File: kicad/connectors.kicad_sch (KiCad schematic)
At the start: 5 parts, among them J1 Conn_Coaxial, J2 Conn_Coaxial, J3 Conn_Coaxial, J4 Conn_Coaxial, J7 Conn_Coaxial

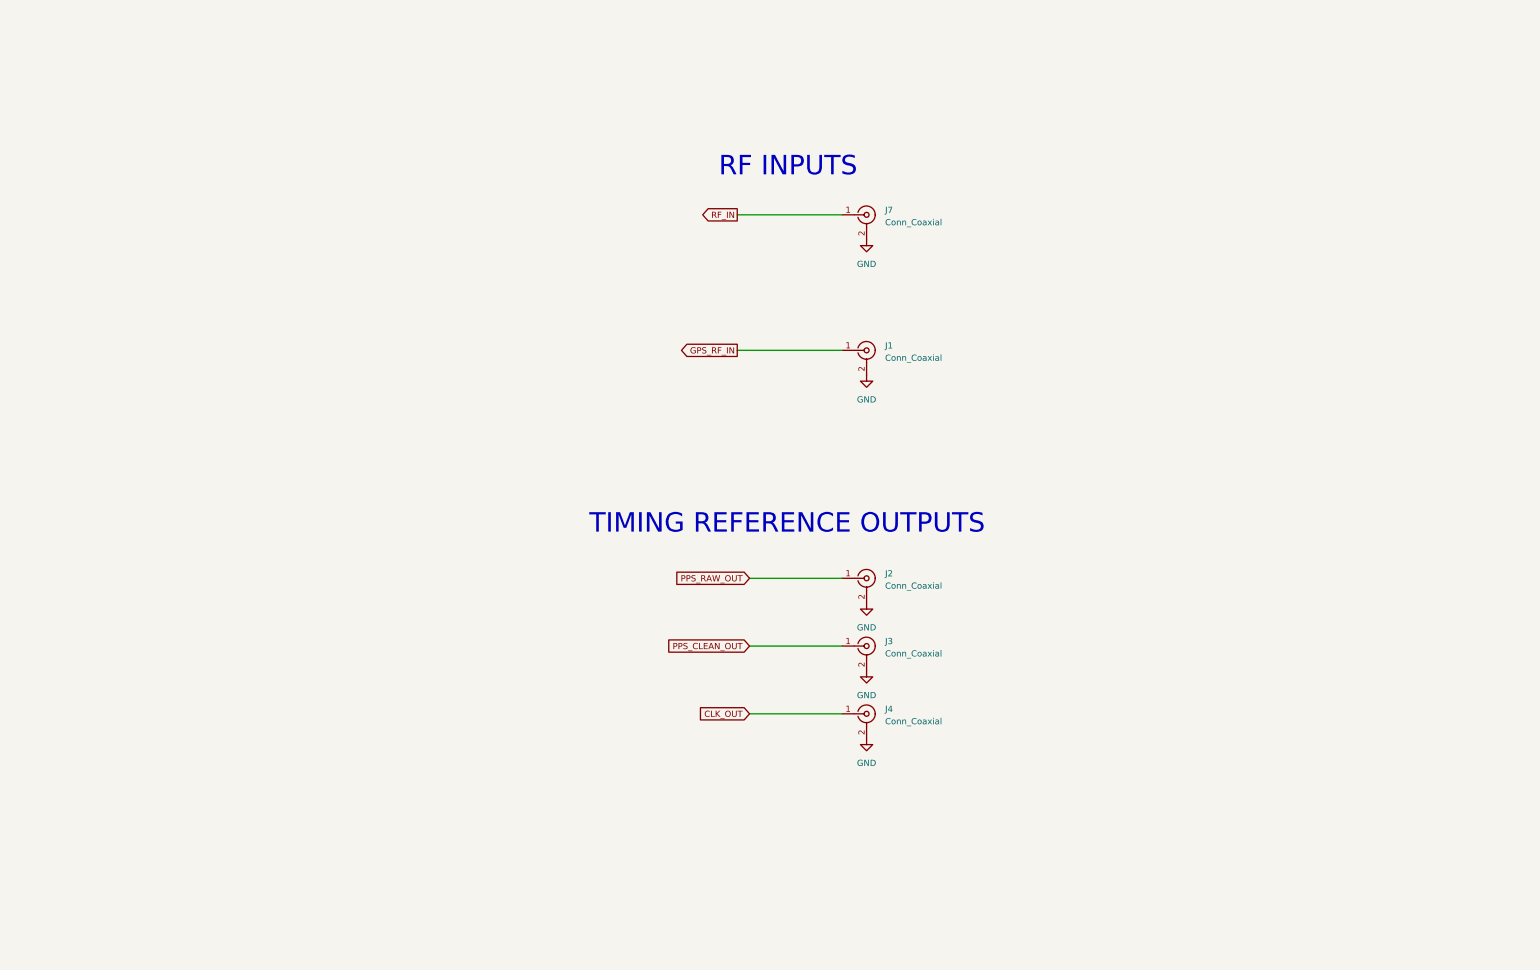
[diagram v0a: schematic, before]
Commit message: swap ice40 for max v, add 1.2v switcher
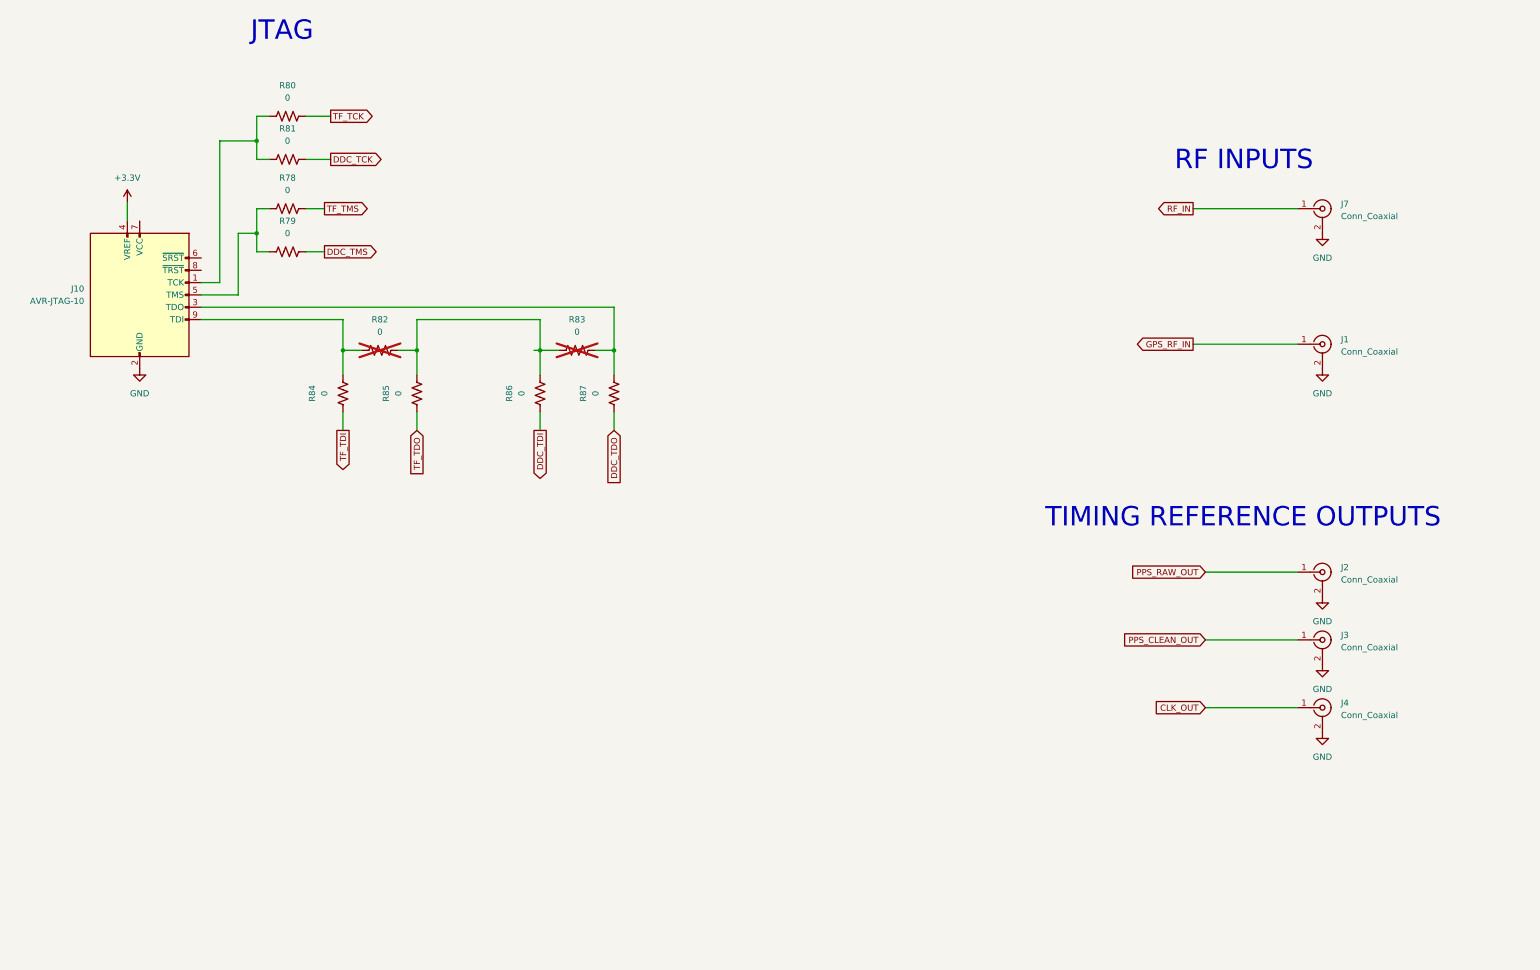
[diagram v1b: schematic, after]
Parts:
- added J10: AVR-JTAG-10, symbol Connector:AVR-JTAG-10
- added R78, R79, R80, R81, R82, R83, R84, R85, R86, R87: 0, symbol Device:R_US
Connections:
- net GND: now also J10.10 (GND), J10.2 (GND)
- new net: J10.5 (TMS), R78.1, R79.1
- new net: J10.1 (TCK), R80.1, R81.1
- new net: J10.3 (TDO), R83.2, R87.2
- new net: J10.9 (TDI), R82.1, R84.2
- new net: R82.2, R83.1, R85.2, R86.2
- new net +3.3V: J10.4 (VREF)
- new net DDC_TCK: R81.2
- new net DDC_TDI: R86.1
- new net DDC_TDO: R87.1
- new net DDC_TMS: R79.2
- new net TF_TCK: R80.2
- new net TF_TDI: R84.1
- new net TF_TDO: R85.1
- new net TF_TMS: R78.2
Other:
- note added: "JTAG"
- moved on the sheet: J1, J2, J3, J4, J7

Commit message: add lte radio and various fixes
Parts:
- added J12: Conn_Coaxial, symbol Connector:Conn_Coaxial
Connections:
- net GND: now also J12.2 (Ext)
- new net LTE_ANT: J12.1 (In)
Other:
- moved on the sheet: J1, J10, R78, R79, R80, R81, R82, R83, R84, R85, R86, R87

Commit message: assign footprints
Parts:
- J1, J12, J2, J3, J4, J7: footprint (none) -> Connector_Coaxial:SMA_Amphenol_901-143_Horizontal
- J10: footprint (none) -> Connector_PinHeader_2.54mm:PinHeader_2x05_P2.54mm_Vertical
- R78, R79, R80, R81, R82, R83, R84, R85, R86, R87: footprint (none) -> Resistor_SMD:R_0603_1608Metric_Pad0.98x0.95mm_HandSolder
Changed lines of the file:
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@@
       (effects (font (size 1.27 1.27)))
     )
-    (property "Footprint" "" (at 108.204 120.904 90)
+    (property "Footprint" "Resistor_SMD:R_0603_1608Metric_Pad0.98x0.95mm_HandSolder" (at 108.204 120.904 90)
       (effects (font (size 1.27 1.27)) hide)
     )
@@
       (effects (font (size 1.27 1.27)) (justify left))
     )
-    (property "Footprint" "" (at 318.77 156.21 0)
+    (property "Footprint" "Connector_Coaxial:SMA_Amphenol_901-143_Horizontal" (at 318.77 156.21 0)
       (effects (font (size 1.27 1.27)) hide)
     )
@@
       (effects (font (size 1.27 1.27)) (justify right))
     )
-    (property "Footprint" "" (at 73.66 135.89 90)
+    (property "Footprint" "Connector_PinHeader_2.54mm:PinHeader_2x05_P2.54mm_Vertical" (at 73.66 135.89 90)
       (effects (font (size 1.27 1.27)) hide)
     )
@@
       (effects (font (size 1.27 1.27)))
     )
-    (property "Footprint" "" (at 133.604 159.766 90)
+    (property "Footprint" "Resistor_SMD:R_0603_1608Metric_Pad0.98x0.95mm_HandSolder" (at 133.604 159.766 90)
       (effects (font (size 1.27 1.27)) hide)
     )
@@
       (effects (font (size 1.27 1.27)) (justify left))
     )
-    (property "Footprint" "" (at 318.77 81.28 0)
+    (property "Footprint" "Connector_Coaxial:SMA_Amphenol_901-143_Horizontal" (at 318.77 81.28 0)
       (effects (font (size 1.27 1.27)) hide)
     )
@@
       (effects (font (size 1.27 1.27)))
     )
-    (property "Footprint" "" (at 167.894 150.114 90)
+    (property "Footprint" "Resistor_SMD:R_0603_1608Metric_Pad0.98x0.95mm_HandSolder" (at 167.894 150.114 90)
       (effects (font (size 1.27 1.27)) hide)
     )
@@
       (effects (font (size 1.27 1.27)))
     )
-    (property "Footprint" "" (at 127.254 150.114 90)
+    (property "Footprint" "Resistor_SMD:R_0603_1608Metric_Pad0.98x0.95mm_HandSolder" (at 127.254 150.114 90)
       (effects (font (size 1.27 1.27)) hide)
     )
@@
       (effects (font (size 1.27 1.27)))
     )
-    (property "Footprint" "" (at 108.204 101.854 90)
+    (property "Footprint" "Resistor_SMD:R_0603_1608Metric_Pad0.98x0.95mm_HandSolder" (at 108.204 101.854 90)
       (effects (font (size 1.27 1.27)) hide)
     )
@@
       (effects (font (size 1.27 1.27)))
     )
-    (property "Footprint" "" (at 118.364 159.766 90)
+    (property "Footprint" "Resistor_SMD:R_0603_1608Metric_Pad0.98x0.95mm_HandSolder" (at 118.364 159.766 90)
       (effects (font (size 1.27 1.27)) hide)
     )
@@
       (effects (font (size 1.27 1.27)) (justify left))
     )
-    (property "Footprint" "" (at 318.77 104.14 0)
+    (property "Footprint" "Connector_Coaxial:SMA_Amphenol_901-143_Horizontal" (at 318.77 104.14 0)
       (effects (font (size 1.27 1.27)) hide)
     )
@@
       (effects (font (size 1.27 1.27)) (justify left))
     )
-    (property "Footprint" "" (at 318.77 170.18 0)
+    (property "Footprint" "Connector_Coaxial:SMA_Amphenol_901-143_Horizontal" (at 318.77 170.18 0)
       (effects (font (size 1.27 1.27)) hide)
     )
@@
       (effects (font (size 1.27 1.27)) (justify left))
     )
-    (property "Footprint" "" (at 318.77 128.27 0)
+    (property "Footprint" "Connector_Coaxial:SMA_Amphenol_901-143_Horizontal" (at 318.77 128.27 0)
       (effects (font (size 1.27 1.27)) hide)
     )
@@
       (effects (font (size 1.27 1.27)))
     )
-    (property "Footprint" "" (at 108.204 129.794 90)
+    (property "Footprint" "Resistor_SMD:R_0603_1608Metric_Pad0.98x0.95mm_HandSolder" (at 108.204 129.794 90)
       (effects (font (size 1.27 1.27)) hide)
     )
@@
       (effects (font (size 1.27 1.27)))
     )
-    (property "Footprint" "" (at 108.204 110.744 90)
+    (property "Footprint" "Resistor_SMD:R_0603_1608Metric_Pad0.98x0.95mm_HandSolder" (at 108.204 110.744 90)
       (effects (font (size 1.27 1.27)) hide)
     )
@@
       (effects (font (size 1.27 1.27)) (justify left))
     )
-    (property "Footprint" "" (at 318.77 184.15 0)
+    (property "Footprint" "Connector_Coaxial:SMA_Amphenol_901-143_Horizontal" (at 318.77 184.15 0)
       (effects (font (size 1.27 1.27)) hide)
     )
@@
       (effects (font (size 1.27 1.27)))
     )
-    (property "Footprint" "" (at 174.244 159.766 90)
+    (property "Footprint" "Resistor_SMD:R_0603_1608Metric_Pad0.98x0.95mm_HandSolder" (at 174.244 159.766 90)
       (effects (font (size 1.27 1.27)) hide)
     )
@@
       (effects (font (size 1.27 1.27)))
     )
-    (property "Footprint" "" (at 159.004 159.766 90)
-      (effects (font (size 1.27 1.27)) hide)
-    )
+    (property "Footprint" "Resistor_SMD:R_0603_1608Metric_Pad0.98x0.95mm_HandSolder" (at 159.004 159.766 90)
+      (effects (font (size 1.27 1.27)) hide)
+    )

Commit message: fix ercs
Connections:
- no-connect marks 0 -> 3
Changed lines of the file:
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@@
   (junction (at 160.02 151.13) (diameter 0) (color 0 0 0 0)
   )
+  (no_connect (at 90.17 134.62))
+  (no_connect (at 77.47 124.46))
+  (no_connect (at 90.17 132.08))
   (wire (pts (xy 160.02 151.13) (xy 163.83 151.13))
     (stroke (width 0) (type default))

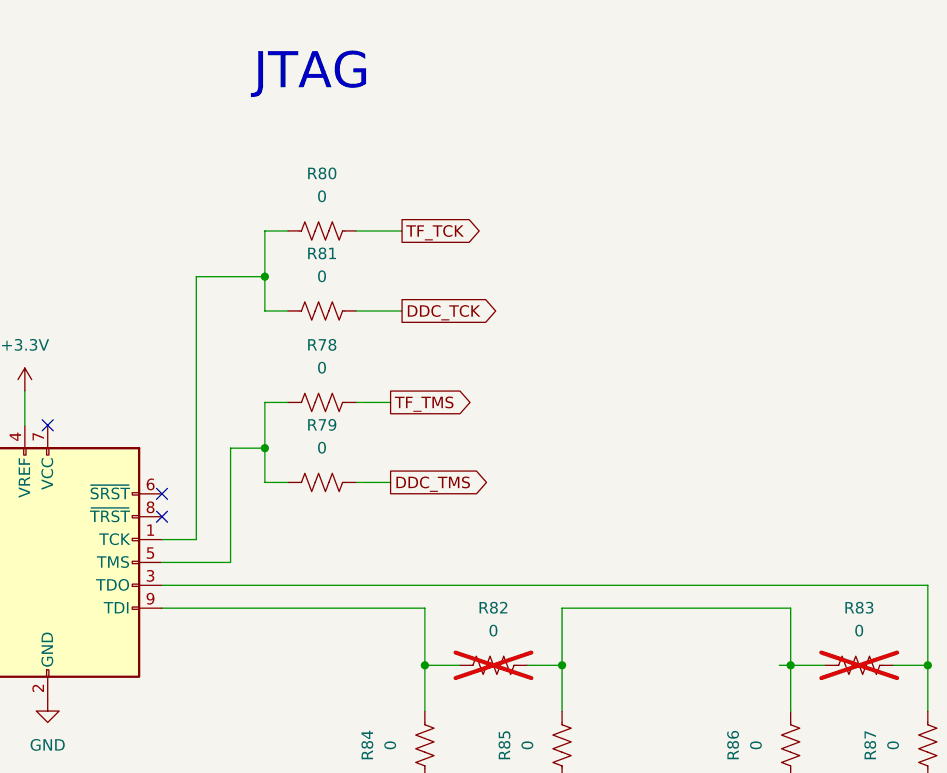
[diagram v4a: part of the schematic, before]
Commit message: add net names
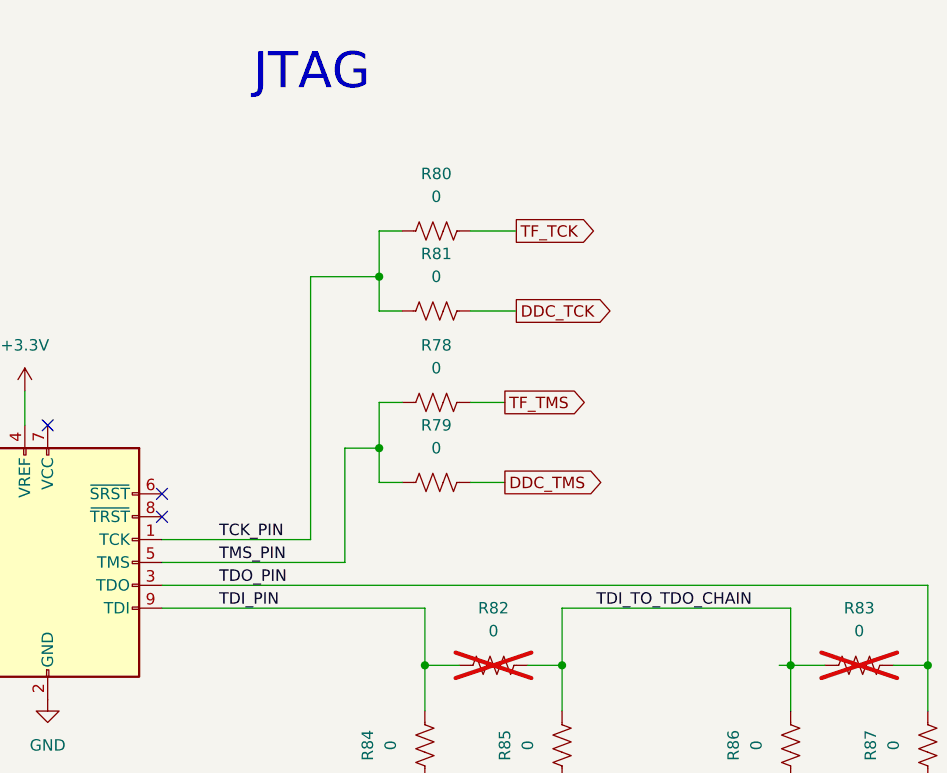
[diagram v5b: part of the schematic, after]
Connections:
- net TMS_PIN: now reaches J10.5 (TMS), R78.1, R79.1
- net TCK_PIN: now reaches J10.1 (TCK), R80.1, R81.1
- net TDO_PIN: now reaches J10.3 (TDO), R83.2, R87.2
- net TDI_PIN: now reaches J10.9 (TDI), R82.1, R84.2
- net TDI_TO_TDO_CHAIN: now reaches R82.2, R83.1, R85.2, R86.2
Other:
- moved on the sheet: R78, R79, R80, R81

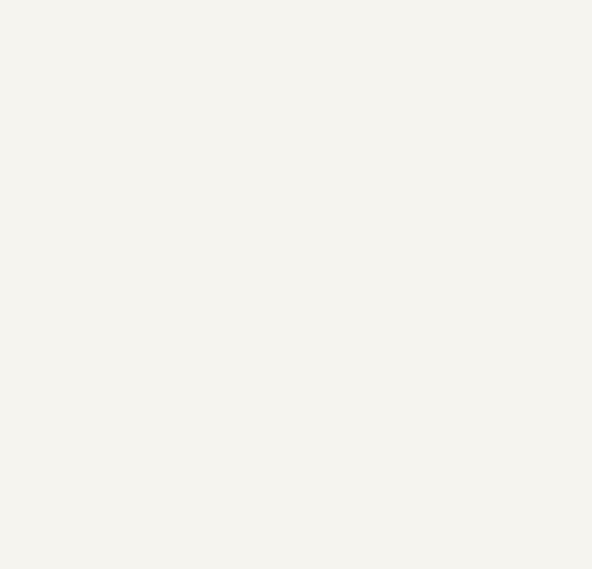
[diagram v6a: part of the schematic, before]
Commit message: fix schematic to align w/ pcb
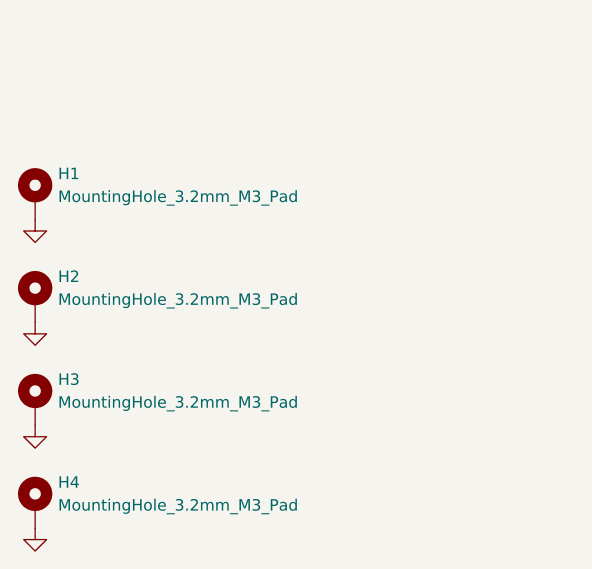
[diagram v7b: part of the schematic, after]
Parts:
- added H1, H2, H3, H4: MountingHole_3.2mm_M3_Pad, MountingHole:MountingHole_3.2mm_M3_Pad, symbol Mechanical:MountingHole_Pad
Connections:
- net GND: now also H1.1, H2.1, H3.1, H4.1

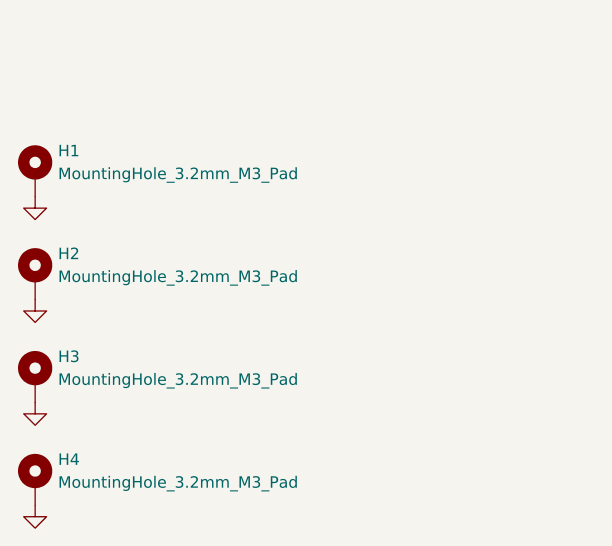
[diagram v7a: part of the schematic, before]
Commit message: fix hoel name
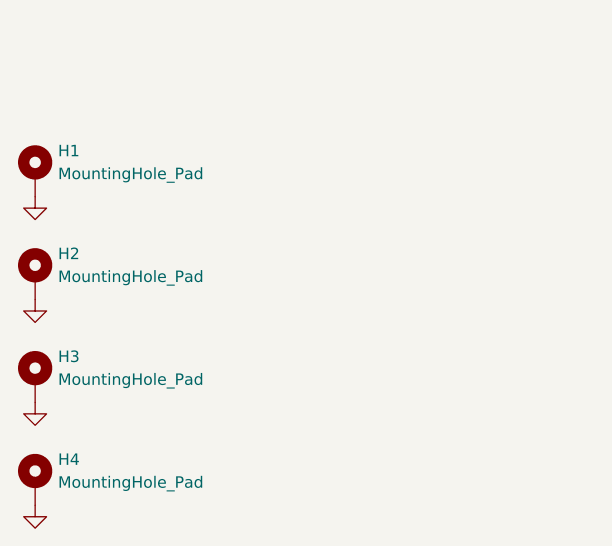
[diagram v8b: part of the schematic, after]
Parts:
- H1, H2, H3, H4: value MountingHole_3.2mm_M3_Pad -> MountingHole_Pad
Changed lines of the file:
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@@
 			)
 		)
-		(property "Value" "MountingHole_3.2mm_M3_Pad"
+		(property "Value" "MountingHole_Pad"
 			(at 53.34 208.2799 0)
 			(effects
@@
 			)
 		)
-		(property "Value" "MountingHole_3.2mm_M3_Pad"
+		(property "Value" "MountingHole_Pad"
 			(at 53.34 231.1399 0)
 			(effects
@@
 			)
 		)
-		(property "Value" "MountingHole_3.2mm_M3_Pad"
+		(property "Value" "MountingHole_Pad"
 			(at 53.34 219.7099 0)
 			(effects
@@
 			)
 		)
-		(property "Value" "MountingHole_3.2mm_M3_Pad"
+		(property "Value" "MountingHole_Pad"
 			(at 53.34 196.8499 0)
 			(effects
